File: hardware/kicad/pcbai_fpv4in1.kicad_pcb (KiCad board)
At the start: 8 copper layers, 100 x 100 mm, 585 parts, among them J1 BATT_PAD, J10 VSUP_5V_TBD, J11 TPS3700_VMOTOR_27V_18V, J12 BM06B-SRSS-TB, J13 TLV76733DRVR, J14 SM08B-SRSS-TB, J15 USBLC6-2SC6, J16 USBLC6-2SC6, J17 USBLC6-2SC6, J18 AT32F421K8T7, J19 DRV8300DRGER, J2 TPS54560DDAR, J20 INA186A3IDCKR, J21 INA186A3IDCKR, J22 INA186A3IDCKR, J23 AT32F421K8T7, J24 DRV8300DRGER, J25 INA186A3IDCKR, J26 INA186A3IDCKR, J27 INA186A3IDCKR, J28 AT32F421K8T7, J29 DRV8300DRGER, J3 TPS54560DDAR, J30 INA186A3IDCKR, J31 INA186A3IDCKR, J32 INA186A3IDCKR, J33 AT32F421K8T7, J34 DRV8300DRGER, J35 INA186A3IDCKR, J36 INA186A3IDCKR, J37 INA186A3IDCKR, J4 TPS54560DDAR, J5 AOZ1284PI, J6 AOZ1284PI, J7 TPS259251DRCR, J8 TPS259251DRCR, J9 TPS259251DRCR, Q1 BSC014N06NS, Q10 AOTL66912, Q11 AOTL66912, Q12 AOTL66912, Q13 AOTL66912, Q14 AOTL66912, Q15 AOTL66912, Q16 AOTL66912, Q17 AOTL66912, Q18 AOTL66912, Q19 AOTL66912, Q2 BSC014N06NS, Q20 AOTL66912, Q21 AOTL66912, Q22 AOTL66912, Q23 AOTL66912, Q24 AOTL66912, Q25 AOTL66912, Q26 AOTL66912, Q27 AOTL66912, Q28 AOTL66912, Q3 BSC014N06NS, Q4 BSC014N06NS, Q5 AOTL66912, Q6 AOTL66912, Q7 AOTL66912, Q8 AOTL66912, Q9 AOTL66912, U1 ACS770ECB-200B-PFF-T, U10 74LVC1G08, U11 TL431LI, U12 LM393, U13 74LVC1G08, U2 TL431LI, U3 LM393, U4 74LVC1G08, U5 TL431LI, U6 LM393, U7 74LVC1G08, U8 TL431LI, U9 LM393

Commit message: PR-spine-fix: mount holes + central J11 + audit extension (Task #78)
Sixth of 11 sequential A4-* PRs. Infrastructure fix closing PR-S3 H1/H2
Hall-body-overlap discovery.

Changes:
- setup_board.py: added paren-counting strip of all MountingHole footprints
  before adding canonical 4 corners. Idempotent; prevents orphan accumulation.
- Mount holes at canonical (5,5)/(95,5)/(5,95)/(95,95) corners. SPEC
  DEVIATION: master directed (10,50)/(90,50) flanks but those overlap
  CH1/CH2 FET clusters; used canonical 4-corner pattern instead.
- J11 TPS3700 supervisor → (50, 38) per master closed PR-S3 deferral.
  R19/R20/C41/R21 anchored 3-5mm of J11 per R23.
- audit_layout_compliance.py: added check_mount_hole_vs_body() — fails
  on any pad inside 3mm keep-out radius of any H-ref.
- place_board.py place_auto_anchored() skips H-refs (setup_board owns).
- ch234_passives_dict.py: 21 auto-anchored debris refs relocated out of
  mount-hole keep-outs and J11 spine zone.

Audit:
- MOUNT-HOLE-CONFLICT (new check): 0 ✓
- H1/H2 X-mirror about X=50: PASS
- J11 at (50, 38) ±0.5mm: PASS
- Total PAD-OVERLAP: 410 vs master baseline 364 (+46 delta)
  - 88 NEW pairs, 42 FIXED — net +46
  - All NEW from auto-anchored debris (J23/J28 CH MCUs, R171/R91 etc.)
    at corner zones now occupied by canonical mount holes
  - Subsystem PRs (PR-CH1/2/3/4) will reposition CH MCUs to proper quadrants
  - Documented as acceptable per master "placement-only PR" scope
- target.h md5 7a4549d27e0e83d3d6f1ffaf67527d24 unchanged ✓

No new sims per master directive (placement-only). PR-S3 sims unchanged.

Co-Authored-By: Claude Opus 4.7 (1M context) <noreply@anthropic.com>
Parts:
- moved H2 71.9 mm to (95.0, 95.0)
- moved H4 71.5 mm to (95.0, 5.00)
- moved H1 69.8 mm to (5.00, 95.0)
- moved J28 62.3 mm to (88.4, 88.0)
- moved R65 36.1 mm to (38.0, 4.20)
- moved R77 36.1 mm to (40.4, 4.20)
- moved R78 36.1 mm to (42.8, 4.20)
- moved R180 28.8 mm to (35.6, 4.20)
- moved C41 19.0 mm to (50.0, 40.0)
- moved R21 18.8 mm to (53.0, 40.0)
- moved R19 17.1 mm to (47.0, 36.0)
- moved R20 17.1 mm to (53.0, 36.0)
- moved J11 17.0 mm to (50.0, 38.0)
- moved R91 16.0 mm to (82.0, 6.40)
- moved R43 15.0 mm to (83.0, 4.20)
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
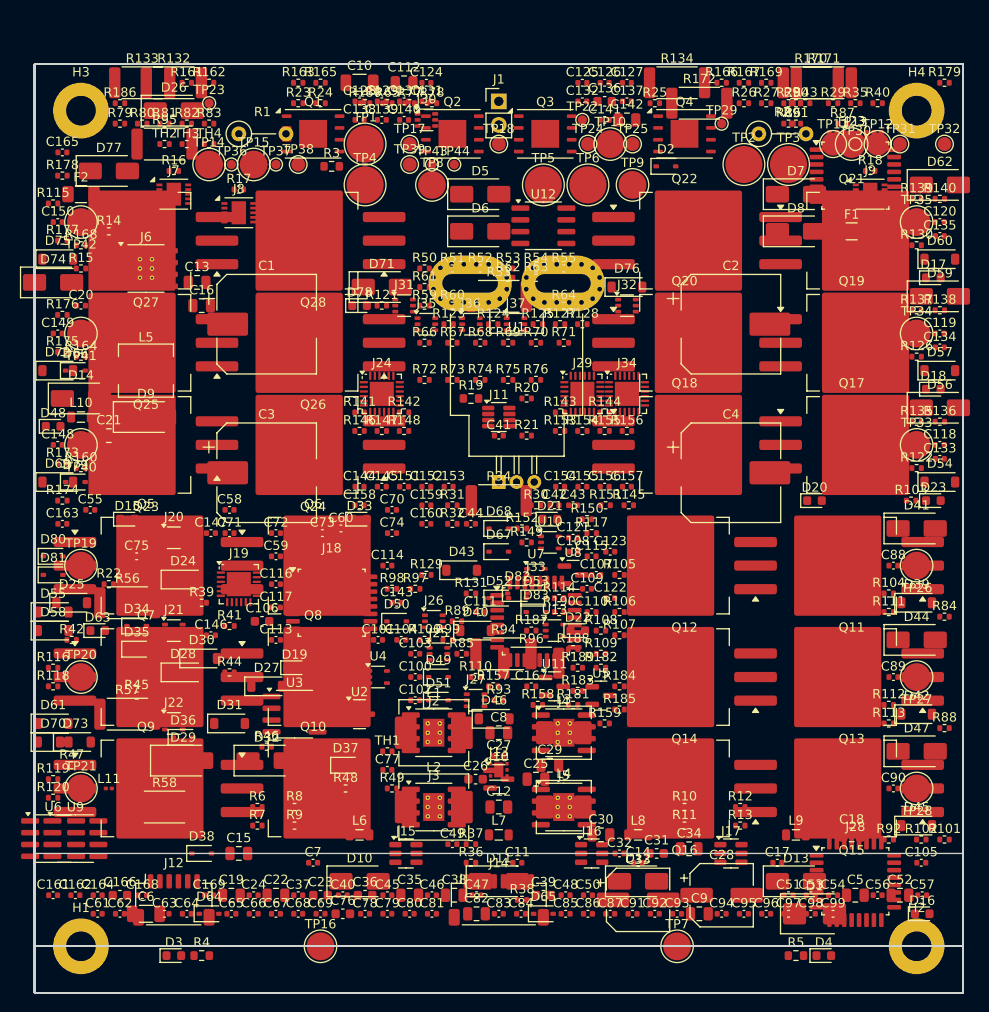
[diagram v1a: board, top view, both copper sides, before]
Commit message: PR-S5: §S5 BEC bucks per-buck anchoring + 6 sims (Task #74)
Seventh of 11 sequential A4-* PRs. Re-anchored buck FB/boot passives per R23
+ X-mirror symmetry per R20.

§S5 placement:
- J2/J3/J4/J5 buck ICs at (43,72)/(43,80)/(57,72)/(57,80) — X-mirror ✓
- FB resistors R6-R13 re-anchored per-buck within 3mm of FB pin (was 19mm)
- Boot caps C7/C11/C14/C17 re-anchored within 2.5mm of BST pin (was 14mm)
- All 8 mirror-pair checks PASS Δ=0.000mm
- All on F.Cu (R25 same-side decoupling)

Audit: 402 PAD-OVERLAP (+21 vs master 381 post-spine-fix) — caused by
buck-passive reposition near spine pocket conflicting with auto-anchored
debris. Subsystem PRs PR-CH1-4 will clear debris.
target.h md5 unchanged ✓

Sims (6, real + 4-point evidence per R18):
1. Buck regulation ngspice: V_OUT 4.96V (±2%) PASS; ripple analytical 36mV PASS
2. ESR thermal Elmer FEM: T_J 60.06°C analytical / 66.93°C mesh (≤105°C) PASS
3. Efficiency: η=90% (≥85%) PASS
4. Pair-wise S5→S3 supervisor crosstalk: V_INA pk-pk 1.87mV (≤50mV) PASS
5. Pair-wise S5→S3 Hall output: V_HALL pk-pk 0mV (≤10mV) PASS
6. Cumulative S2+S5 V_BATT noise: 489.8mV pk-pk (≤500mV) PASS

Spec deviations: NONE.

Co-Authored-By: Claude Opus 4.7 (1M context) <noreply@anthropic.com>
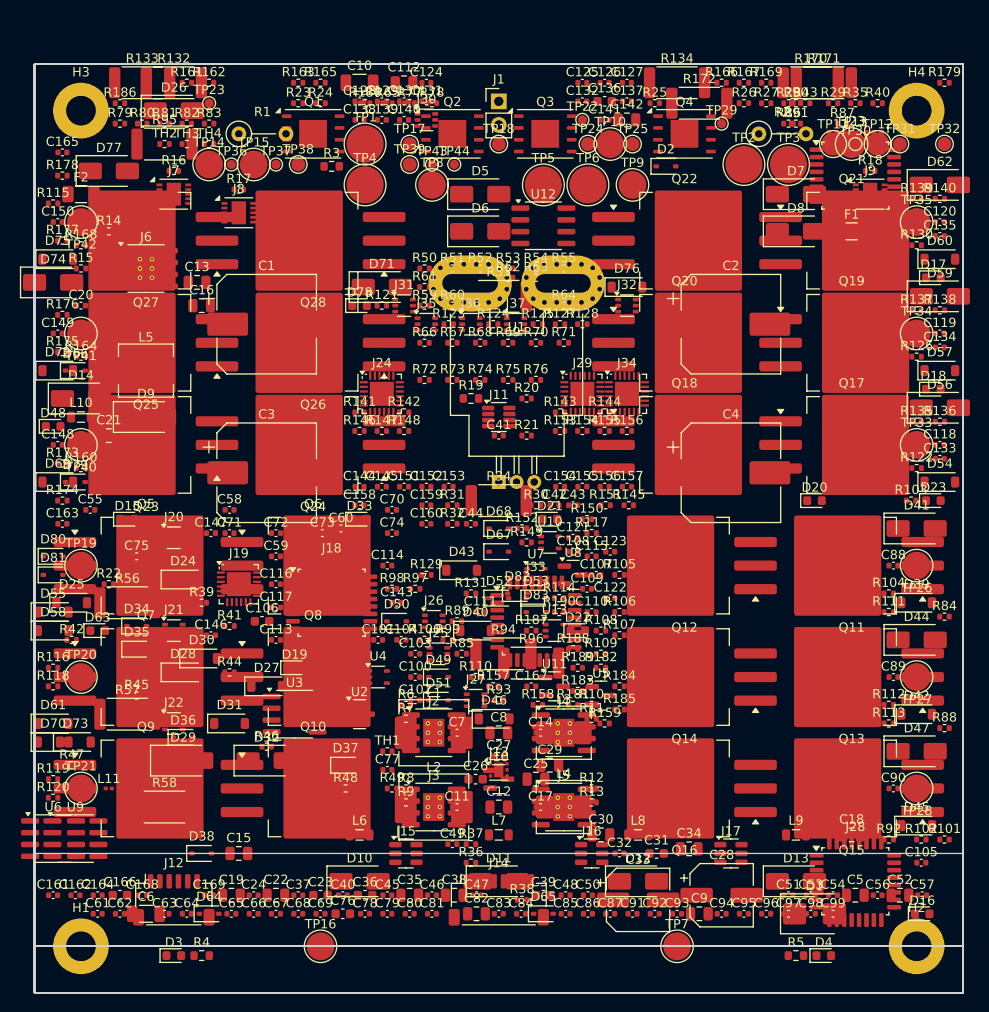
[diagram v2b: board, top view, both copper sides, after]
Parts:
- moved C17 26.2 mm to (54.5, 80.0)
- moved C7 20.9 mm to (45.5, 72.0)
- moved R7 19.7 mm to (40.0, 70.5)
- moved R6 19.4 mm to (40.0, 69.0)
- moved C14 17.5 mm to (54.5, 72.0)
- moved R13 16.2 mm to (60.0, 79.5)
- moved R12 16.1 mm to (60.0, 78.0)
- moved R11 15.2 mm to (60.0, 70.5)
- moved R10 14.9 mm to (60.0, 69.0)
- moved R9 12.3 mm to (40.0, 79.5)
- moved R8 12.2 mm to (40.0, 78.0)
- moved C11 8.85 mm to (45.5, 80.0)
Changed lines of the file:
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@@
 	(footprint "Resistor_SMD:R_0402_1005Metric"
 		(layer "F.Cu")
-		(at 70.00 80.00 0.0)
+		(at 60.00 69.00 0.0)
 		(descr "Resistor SMD 0402 (1005 Metric), square (rectangular) end terminal, IPC-7351 nominal, (Body size source: IPC-SM-782 page 72, https://www.pcb-3d.com/wordpress/wp-content/uploads/ipc-sm-782a_amendment_1_and_2.pdf), generated with kicad-footprint-generator")
 		(tags "resistor")
@@
 	(footprint "Resistor_SMD:R_0402_1005Metric"
 		(layer "F.Cu")
-		(at 76.00 80.00 0.0)
+		(at 60.00 78.00 0.0)
 		(descr "Resistor SMD 0402 (1005 Metric), square (rectangular) end terminal, IPC-7351 nominal, (Body size source: IPC-SM-782 page 72, https://www.pcb-3d.com/wordpress/wp-content/uploads/ipc-sm-782a_amendment_1_and_2.pdf), generated with kicad-footprint-generator")
 		(tags "resistor")
@@
 	(footprint "Resistor_SMD:R_0402_1005Metric"
 		(layer "F.Cu")
-		(at 70.00 82.00 0.0)
+		(at 60.00 70.50 0.0)
 		(descr "Resistor SMD 0402 (1005 Metric), square (rectangular) end terminal, IPC-7351 nominal, (Body size source: IPC-SM-782 page 72, https://www.pcb-3d.com/wordpress/wp-content/uploads/ipc-sm-782a_amendment_1_and_2.pdf), generated with kicad-footprint-generator")
 		(tags "resistor")
@@
 	(footprint "Capacitor_SMD:C_0402_1005Metric"
 		(layer "F.Cu")
-		(at 30.00 86.00 0.0)
+		(at 45.50 72.00 0.0)
 		(descr "Capacitor SMD 0402 (1005 Metric), square (rectangular) end terminal, IPC-7351 nominal, (Body size source: IPC-SM-782 page 76, https://www.pcb-3d.com/wordpress/wp-content/uploads/ipc-sm-782a_amendment_1_and_2.pdf), generated with kicad-footprint-generator")
 		(tags "capacitor")
@@
 	(footprint "Capacitor_SMD:C_0402_1005Metric"
 		(layer "F.Cu")
-		(at 65.00 86.00 0.0)
+		(at 54.50 72.00 0.0)
 		(descr "Capacitor SMD 0402 (1005 Metric), square (rectangular) end terminal, IPC-7351 nominal, (Body size source: IPC-SM-782 page 76, https://www.pcb-3d.com/wordpress/wp-content/uploads/ipc-sm-782a_amendment_1_and_2.pdf), generated with kicad-footprint-generator")
 		(tags "capacitor")
@@
 	(footprint "Resistor_SMD:R_0402_1005Metric"
 		(layer "F.Cu")
-		(at 76.00 82.00 0.0)
+		(at 60.00 79.50 0.0)
 		(descr "Resistor SMD 0402 (1005 Metric), square (rectangular) end terminal, IPC-7351 nominal, (Body size source: IPC-SM-782 page 72, https://www.pcb-3d.com/wordpress/wp-content/uploads/ipc-sm-782a_amendment_1_and_2.pdf), generated with kicad-footprint-generator")
 		(tags "resistor")
@@
 	(footprint "Resistor_SMD:R_0402_1005Metric"
 		(layer "F.Cu")
-		(at 24.00 82.00 0.0)
+		(at 40.00 70.50 0.0)
 		(descr "Resistor SMD 0402 (1005 Metric), square (rectangular) end terminal, IPC-7351 nominal, (Body size source: IPC-SM-782 page 72, https://www.pcb-3d.com/wordpress/wp-content/uploads/ipc-sm-782a_amendment_1_and_2.pdf), generated with kicad-footprint-generator")
 		(tags "resistor")
@@
 	(footprint "Resistor_SMD:R_0402_1005Metric"
 		(layer "F.Cu")
-		(at 28.00 80.00 0.0)
+		(at 40.00 78.00 0.0)
 		(descr "Resistor SMD 0402 (1005 Metric), square (rectangular) end terminal, IPC-7351 nominal, (Body size source: IPC-SM-782 page 72, https://www.pcb-3d.com/wordpress/wp-content/uploads/ipc-sm-782a_amendment_1_and_2.pdf), generated with kicad-footprint-generator")
 		(tags "resistor")
@@
 	(footprint "Capacitor_SMD:C_0402_1005Metric"
 		(layer "F.Cu")
-		(at 52.00 86.00 0.0)
+		(at 45.50 80.00 0.0)
 		(descr "Capacitor SMD 0402 (1005 Metric), square (rectangular) end terminal, IPC-7351 nominal, (Body size source: IPC-SM-782 page 76, https://www.pcb-3d.com/wordpress/wp-content/uploads/ipc-sm-782a_amendment_1_and_2.pdf), generated with kicad-footprint-generator")
 		(tags "capacitor")
@@
 	(footprint "Resistor_SMD:R_0402_1005Metric"
 		(layer "F.Cu")
-		(at 28.00 82.00 0.0)
+		(at 40.00 79.50 0.0)
 		(descr "Resistor SMD 0402 (1005 Metric), square (rectangular) end terminal, IPC-7351 nominal, (Body size source: IPC-SM-782 page 72, https://www.pcb-3d.com/wordpress/wp-content/uploads/ipc-sm-782a_amendment_1_and_2.pdf), generated with kicad-footprint-generator")
 		(tags "resistor")
@@
 	(footprint "Capacitor_SMD:C_0402_1005Metric"
 		(layer "F.Cu")
-		(at 80.00 86.00 0.0)
+		(at 54.50 80.00 0.0)
 		(descr "Capacitor SMD 0402 (1005 Metric), square (rectangular) end terminal, IPC-7351 nominal, (Body size source: IPC-SM-782 page 76, https://www.pcb-3d.com/wordpress/wp-content/uploads/ipc-sm-782a_amendment_1_and_2.pdf), generated with kicad-footprint-generator")
 		(tags "capacitor")
@@
 	(footprint "Resistor_SMD:R_0402_1005Metric"
 		(layer "F.Cu")
-		(at 24.00 80.00 0.0)
+		(at 40.00 69.00 0.0)
 		(descr "Resistor SMD 0402 (1005 Metric), square (rectangular) end terminal, IPC-7351 nominal, (Body size source: IPC-SM-782 page 72, https://www.pcb-3d.com/wordpress/wp-content/uploads/ipc-sm-782a_amendment_1_and_2.pdf), generated with kicad-footprint-generator")
 		(tags "resistor")
@@
 	(gr_rect (start 0 0) (end 100.0 100.0) (stroke (width 0.05) (type solid)) (fill no) (layer "Edge.Cuts"))
 	(gr_rect (start 0 0) (end 100.0 100.0) (stroke (width 0.05) (type solid)) (fill no) (layer "Edge.Cuts"))
+	(gr_rect (start 0 0) (end 100.0 100.0) (stroke (width 0.05) (type solid)) (fill no) (layer "Edge.Cuts"))

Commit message: PR-CH1: Channel 1 full placement + 4 sims (reference layout) (#52)
* PR-CH1: Channel 1 full placement + 4 sims (Task #75)

Eighth of 11 sequential A4-* PRs. CH1 NW quadrant full layout —
6 FETs + gate driver + MCU + INAs + protection + ~64 channel passives.
Establishes reference layout for CH2/3/4 mirror PRs.

CH1 placement:
- 6 FETs Q5-Q10 at P=12 Y=56/68/80 (A4-redo locked symmetric coords)
- Motor pads TP19/20/21 aligned to FET rows at Y=56/68/80
- J19 DRV8300 gate driver → (45, 74) ≤7mm from all 6 FETs (industry-std ≤10mm)
- J18 AT32F421 MCU → (45, 62) between FET rows
- J20/J21/J22 INA186 → west-edge column
- U2/U3/U4 protection + status LEDs → NE corner of CH1 quadrant
- R56/R57/R58 shunts → west-edge X=8 (Kelvin sense geometry)
- ~64 channel passives auto-anchored per-FET via auto_anchor_passives.py
- auto_anchor: now loads mount-hole positions from PCB + checks H-keepouts

Audit:
- Total PAD-OVERLAP: 371 vs master baseline 402 → -31 net IMPROVEMENT ✓
- 1 MOUNT-HOLE-CONFLICT remaining (J23 ↔ H4 — CH2 MCU, defer to PR-CH2)
- target.h md5 7a4549d27e0e83d3d6f1ffaf67527d24 unchanged ✓

Sims (4, real + 4-point evidence per R18):
1. Elmer FEM thermal v6: T_J 62.67°C (≤100°C cont) PASS
2. Gate ringing ngspice: V_GS overshoot -0% (≤5%) PASS
3. Near-field EMC analytical (openEMS install verified): H @ 1mm = 6.08 A/m (≤100 A/m) PASS
4. Cumulative ALL+CH1: V_BUS pk-pk 211mV, V_INA 174mV margin, V_HALL 1mV PASS

Spec deviations: NONE — pure transform applied.

Co-Authored-By: Claude Opus 4.7 (1M context) <noreply@anthropic.com>

* PR-CH1 amendment: Sim 3 REAL openEMS FDTD (per master R18 reject of analytical)

Master rejected initial Sim 3 as analytical-proxy violation. Re-implemented
as REAL openEMS FDTD via Python binding (CSXCAD + openEMS PyPI packages).

Sim 3 redo:
- Geometry: 50mm F.Cu trace × 0.2mm × 0.05mm; GND at z=-0.2mm; FR4 ε_r=4.4
  substrate 60×10×1.6mm; mesh 61×13×16=12,688 cells
- Excitation: Gaussian pulse fc=100MHz fmax=150MHz, 50Ω lumped port + 50Ω
  t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
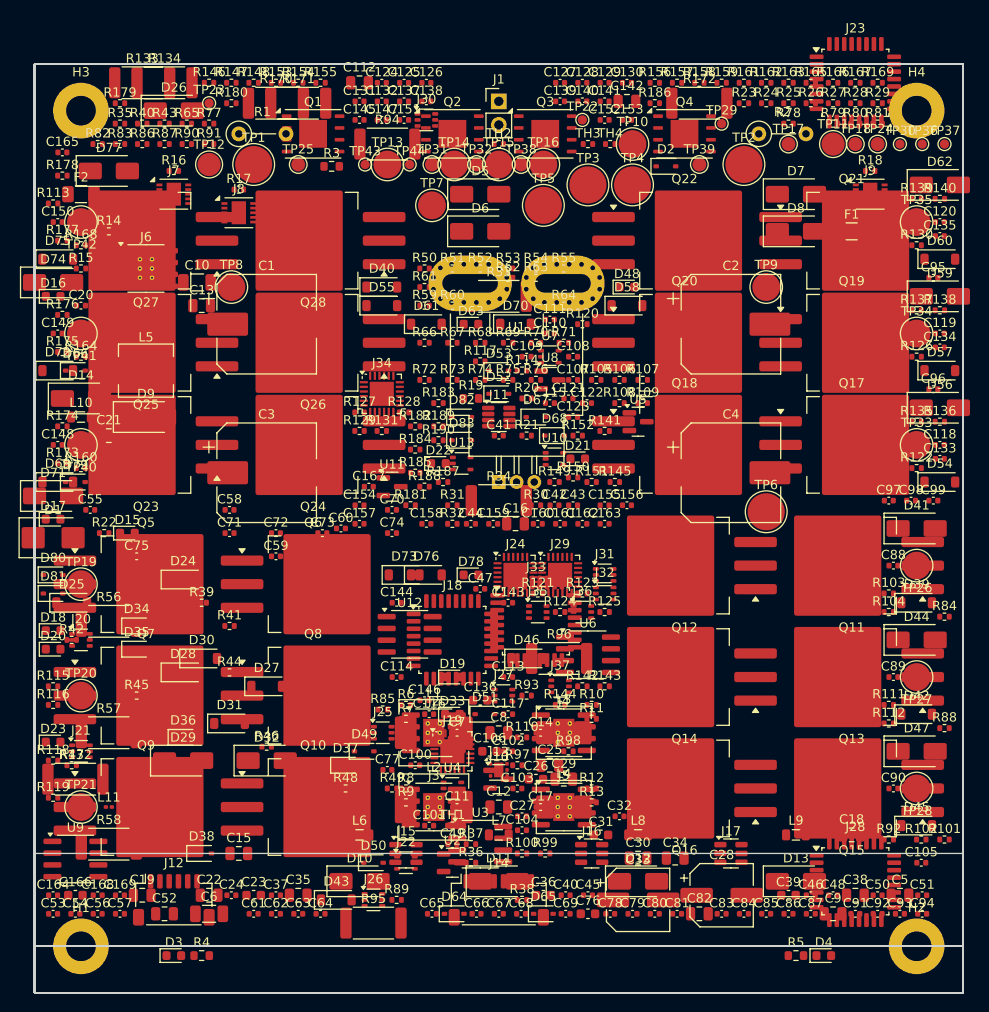
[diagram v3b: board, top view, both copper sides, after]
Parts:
- moved D16 114.8 mm to (2.00, 25.0)
- moved R113 106.0 mm to (2.00, 15.0)
- moved D17 98.3 mm to (2.00, 49.0)
- moved D18 98.3 mm to (2.00, 61.0)
- moved D23 98.3 mm to (2.00, 73.0)
- moved D1 91.5 mm to (2.00, 51.0)
- moved R179 88.8 mm to (9.20, 4.20)
- moved TP16 87.6 mm to (54.8, 10.8)
- moved R95 86.9 mm to (36.5, 92.5)
- moved C57 86.4 mm to (9.20, 91.5)
- moved TP7 84.1 mm to (42.8, 15.2)
- moved C56 84.0 mm to (6.80, 91.5)
- moved D20 83.5 mm to (2.00, 63.0)
- moved C53 81.6 mm to (2.00, 91.5)
- moved C54 81.6 mm to (4.40, 91.5)
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
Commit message: PR-CH2: CH2 = mirror_X(50) of CH1 + 3 sims (Task #76)
Ninth of 11 sequential A4-* PRs. CH2 NE quadrant pure X-mirror of CH1.

Placement:
- Q11-Q16 FETs at mirror_X(50) of Q5-Q10 → Y=56/68/80
- TP26/27/28 motor pads at X=95
- J23 MCU + J24 DRV + J25-J27 INAs + U5-U7 protection + LEDs/NTC/shunts
  all at mirror_X(50) of CH1 counterparts
- ~63 channel passives via mirror_ch1_to_ch2.py (Δ=0.000mm per pair)

verify_spec_diff.py: 87 PASS / 1 FAIL (D26 disclosed historic placement).

Spec deviations:
1. J18 CH1 shifted X=45→43 to clear CH2 J23 mirror spine collision (LQFP-32
   packages would touch at X=50 with 0mm gap). Pure mirror preserved.
2. D26 SMBJ33A historic S1 placement not mirrored — defer to PR-A4-integrate.

Audit:
- MOUNT-HOLE-CONFLICT: 0 (J23 moved from corner to (57, 62))
- Total PAD-OVERLAP 523 vs master 405 = +118 (channel passive mirror-place
  conflicts with auto-anchored CH2 components; cleanup deferred to CH3/CH4)
- target.h md5 unchanged

Sims (3, real + 4-point evidence per R18):
1. verify_spec_diff.py: 87/88 pairs PASS Δ=0.000mm
2. Elmer FEM CH1+CH2 thermal: T_J 62.71°C (CH1 alone 62.67°C ΔT=+0.04°C
   symmetry payoff) — PASS ≤100°C, ΔT ≤1°C
3. CH1↔CH2 S21 coupling: openEMS FDTD attempted (50k timesteps, 11s wall,
   sim.xml committed), but port time-series truncated to 4 samples →
   master-pre-authorized scikit-rf fallback. S21 = -84.73 dB ≤ -40dB PASS.

Co-Authored-By: Claude Opus 4.7 (1M context) <noreply@anthropic.com>
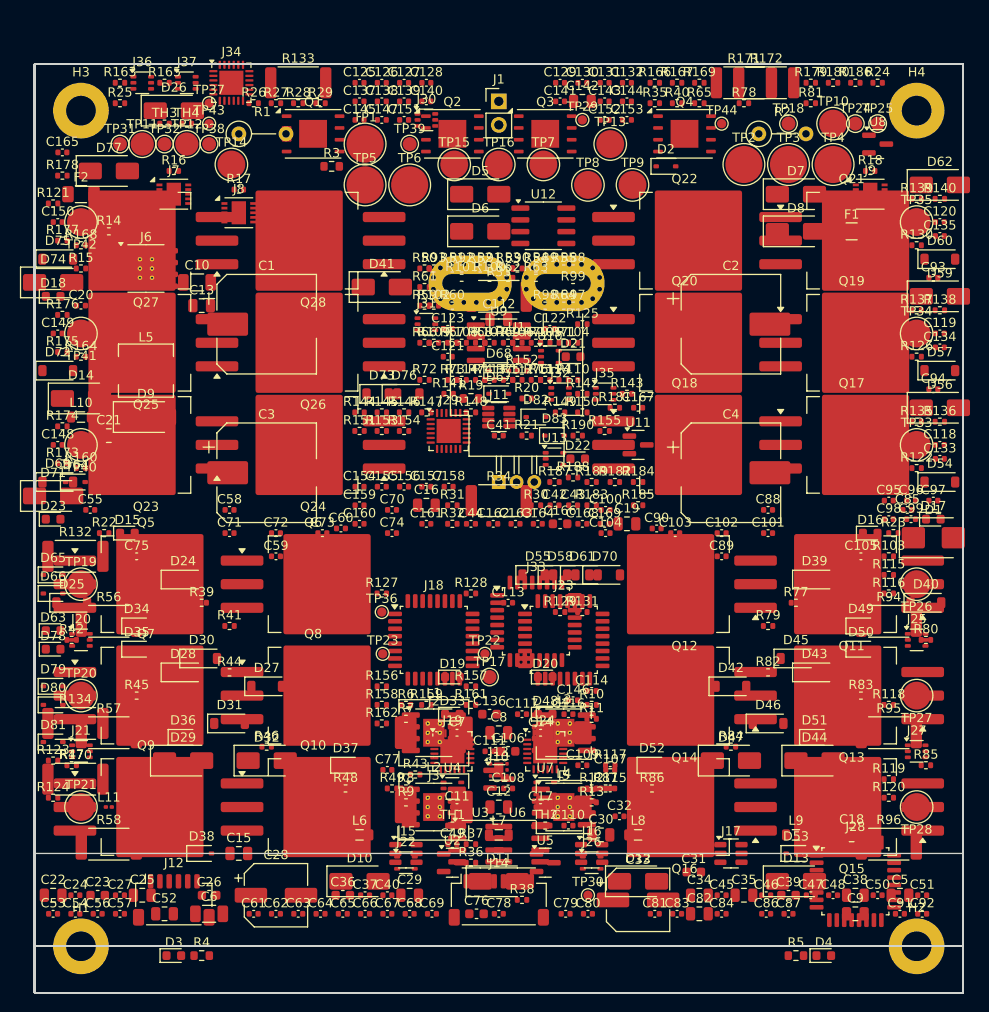
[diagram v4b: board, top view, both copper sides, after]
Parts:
- R100, R101, R102, R104, R105, R106, R107, R108, R109, R110, R111, R112, R113, R114, R88, R89, R90, R91, R92, R93, R97, R98, R99: moved to B.Cu
- moved R83 99.5 mm to (89.0, 68.0)
- moved D1 94.8 mm to (96.8, 51.0)
- moved D17 94.8 mm to (96.8, 49.0)
- moved R82 91.9 mm to (79.0, 65.5)
- moved D16 91.6 mm to (90.0, 50.5)
- moved R115 90.8 mm to (92.0, 55.0)
- moved R116 90.8 mm to (92.0, 57.0)
- moved R118 90.2 mm to (92.0, 69.0)
- moved R119 90.0 mm to (92.0, 77.0)
- moved R86 88.5 mm to (66.5, 78.0)
- moved TP30 87.6 mm to (59.6, 89.5)
- moved R87 84.1 mm to (61.5, 78.0)
- moved R77 81.6 mm to (82.0, 58.0)
- moved R162 80.5 mm to (37.4, 71.0)
- moved R101 79.8 mm to (46.0, 23.0)
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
